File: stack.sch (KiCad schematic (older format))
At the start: 6 parts, among them U26 74LS245, U27 74LS173, U28 74LS173, U29 74LS245, U30 74LS173, U31 74LS173

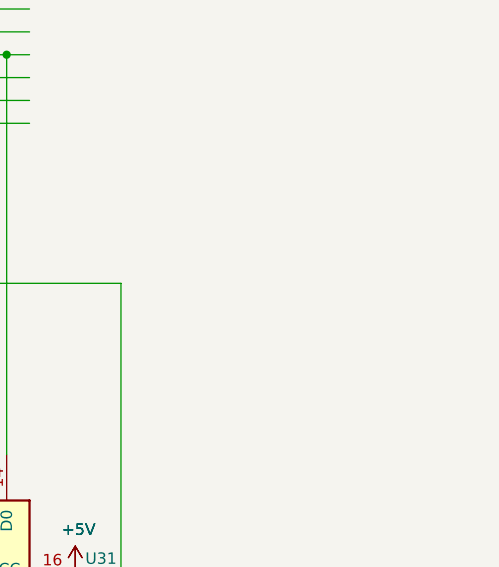
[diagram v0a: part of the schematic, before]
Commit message: added power caps
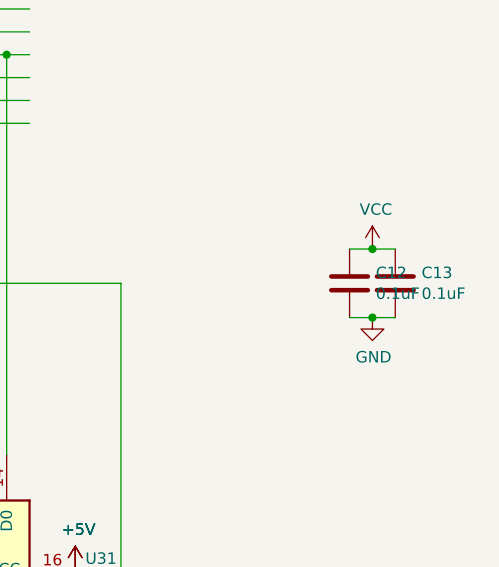
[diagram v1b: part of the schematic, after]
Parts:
- added C12, C13: 0.1uF, Capacitor_THT:CP_Axial_L10.0mm_D4.5mm_P15.00mm_Horizontal, symbol Device:C
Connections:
- net labels added: VCC
- wire segments 251 -> 255
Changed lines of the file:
@@
 $Descr A3 16535 11693
 encoding utf-8
-Sheet 9 21
+Sheet 8 21
 Title ""
 Date ""
@@
 Wire Wire Line
 	7600 3450 8900 3450
+$Comp
+L 16bitCpu-rescue:VCC-power #PWR?
+U 1 1 5FD411B2
+P 11350 2900
+AR Path="/5FD411B2" Ref="#PWR?"  Part="1"
+AR Path="/61968B9B/5FD411B2" Ref="#PWR0265"  Part="1"
+F 0 "#PWR0265" H 11350 2750 50  0001 C CNN
+F 1 "VCC" H 11365 3073 50  0000 C CNN
+F 2 "" H 11350 2900 50  0001 C CNN
+F 3 "" H 11350 2900 50  0001 C CNN
+	1    11350 2900
+	1    0    0    -1
+$EndComp
+$Comp
+L 16bitCpu-rescue:GND-power #PWR?
+U 1 1 5FD411B8
+P 11350 3200
+AR Path="/5FD411B8" Ref="#PWR?"  Part="1"
+AR Path="/5F75E433/5FD411B8" Ref="#PWR?"  Part="1"
+AR Path="/61968B9B/5FD411B8" Ref="#PWR0266"  Part="1"
+F 0 "#PWR0266" H 11350 2950 50  0001 C CNN
+F 1 "GND" H 11355 3027 50  0000 C CNN
+F 2 "" H 11350 3200 50  0001 C CNN
+F 3 "" H 11350 3200 50  0001 C CNN
+	1    11350 3200
+	1    0    0    -1
+$EndComp
+Wire Wire Line
+	11350 2900 11450 2900
+Wire Wire Line
+	11450 3200 11350 3200
+$Comp
+L Device:C C?
+U 1 1 5FD411C0
+P 11250 3050
+AR Path="/5F75E433/5FD411C0" Ref="C?"  Part="1"
+AR Path="/61968B9B/5FD411C0" Ref="C12"  Part="1"
+F 0 "C12" H 11365 3096 50  0000 L CNN
+F 1 "0.1uF" H 11365 3005 50  0000 L CNN
+F 2 "Capacitor_THT:CP_Axial_L10.0mm_D4.5mm_P15.00mm_Horizontal" H 11288 2900 50  0001 C CNN
+F 3 "" H 11250 3050 50  0001 C CNN
+	1    11250 3050
+	1    0    0    -1
+$EndComp
+Wire Wire Line
+	11350 2900 11250 2900
+Connection ~ 11350 2900
+Wire Wire Line
+	11250 3200 11350 3200
+Connection ~ 11350 3200
+$Comp
+L Device:C C?
+U 1 1 5FD411CA
+P 11450 3050
+AR Path="/5F75E433/5FD411CA" Ref="C?"  Part="1"
+AR Path="/61968B9B/5FD411CA" Ref="C13"  Part="1"
+F 0 "C13" H 11565 3096 50  0000 L CNN
+F 1 "0.1uF" H 11565 3005 50  0000 L CNN
+F 2 "Capacitor_THT:CP_Axial_L10.0mm_D4.5mm_P15.00mm_Horizontal" H 11488 2900 50  0001 C CNN
+F 3 "" H 11450 3050 50  0001 C CNN
+	1    11450 3050
+	1    0    0    -1
+$EndComp
 $EndSCHEMATC

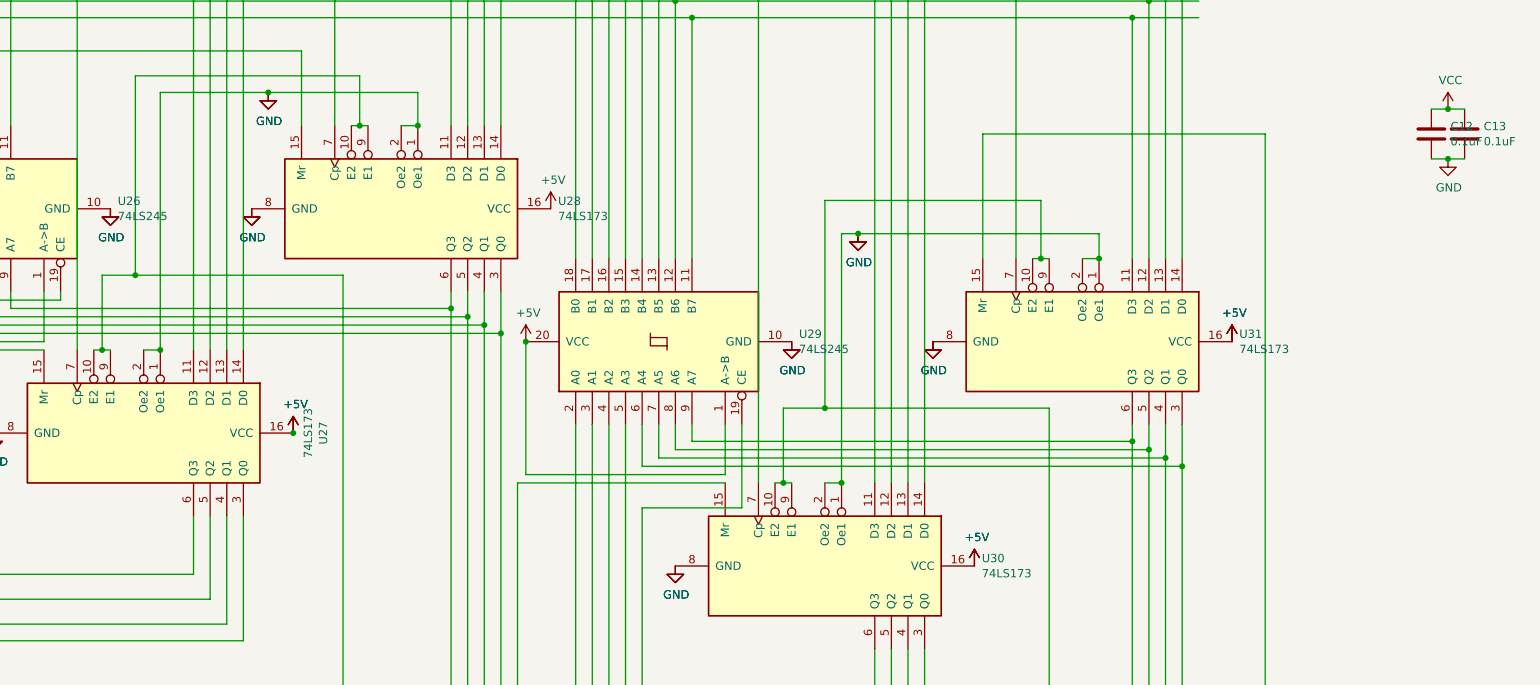
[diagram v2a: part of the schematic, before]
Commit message: added display
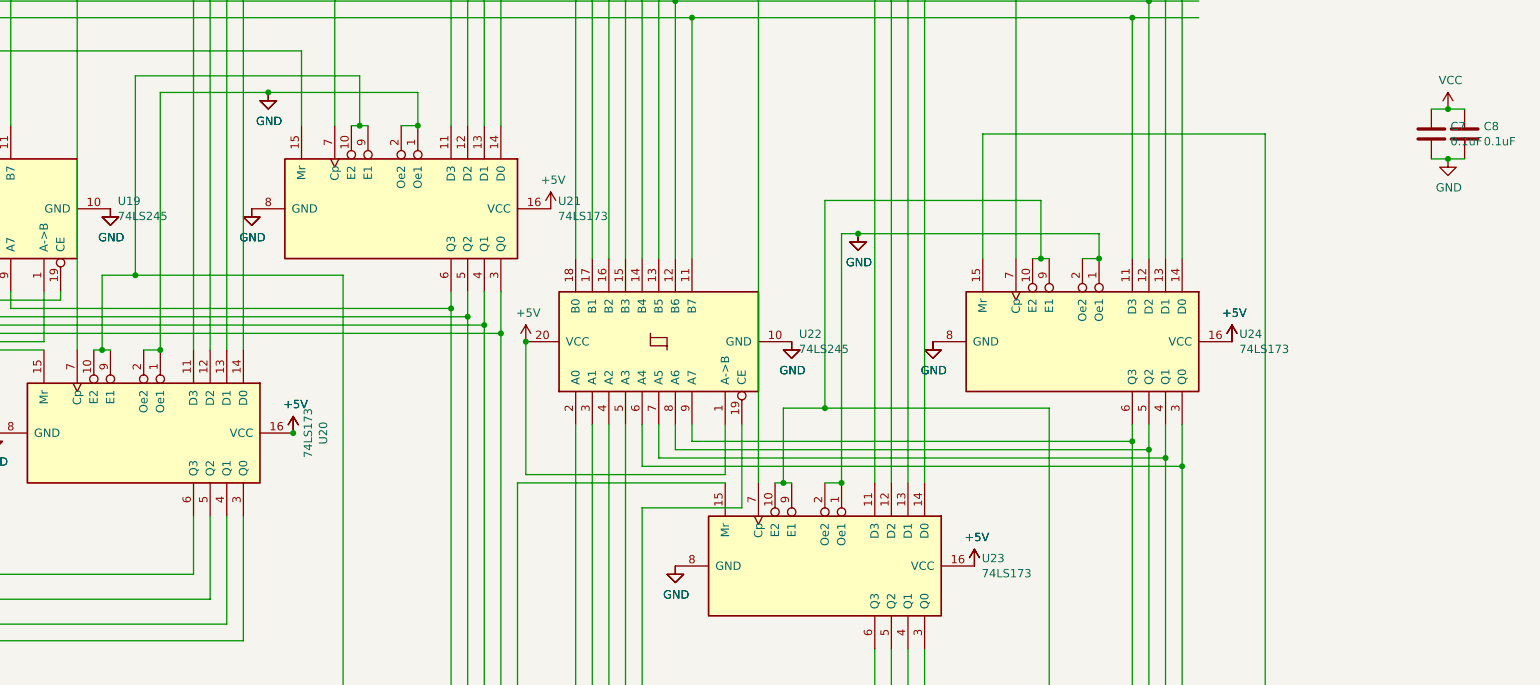
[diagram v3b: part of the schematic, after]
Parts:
- renumbered C12 to C7, C13 to C8, U26 to U19, U27 to U20, U28 to U21, U29 to U22, U30 to U23, U31 to U24

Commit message: clean up
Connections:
- wire segments 255 -> 236
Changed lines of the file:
@@
 Wire Wire Line
 	3800 4350 3800 1150
-Connection ~ 3800 1150
-Connection ~ 3900 1050
-Connection ~ 4000 950
-Connection ~ 4100 850
-Wire Wire Line
-	3900 1050 9850 1050
-Wire Wire Line
-	3800 1150 9850 1150
-Wire Wire Line
-	4000 950  9850 950
-Wire Wire Line
-	4100 850  9850 850
-Connection ~ 5350 1550
-Connection ~ 5450 1450
-Connection ~ 5550 1350
-Connection ~ 5650 1250
-Wire Wire Line
-	5650 1250 9850 1250
-Wire Wire Line
-	5550 1350 9850 1350
-Wire Wire Line
-	5450 1450 9850 1450
-Wire Wire Line
-	5350 1550 9850 1550
 Wire Wire Line
 	1300 1750 6200 1750
@@
 Wire Wire Line
 	6800 2350 9450 2350
-Connection ~ 7900 1950
-Wire Wire Line
-	7900 1950 9850 1950
-Connection ~ 8000 1850
-Wire Wire Line
-	8000 1850 9850 1850
-Connection ~ 8100 1750
-Wire Wire Line
-	8100 1750 9850 1750
-Connection ~ 8200 1650
-Wire Wire Line
-	8200 1650 9850 1650
-Connection ~ 9450 2350
-Wire Wire Line
-	9450 2350 9850 2350
-Connection ~ 9550 2250
-Wire Wire Line
-	9550 2250 9850 2250
-Connection ~ 9650 2150
-Wire Wire Line
-	9650 2150 9850 2150
-Connection ~ 9750 2050
-Wire Wire Line
-	9750 2050 9850 2050
 Wire Wire Line
 	8100 6150 8100 6800
@@
 Wire Wire Line
 	8750 3800 8750 600
-Connection ~ 8750 600
-Wire Wire Line
-	8750 600  9850 600
 Wire Wire Line
 	4650 3000 4650 600
@@
 Wire Wire Line
 	7100 4800 7100 5300
-Connection ~ 6500 8600
-Wire Wire Line
-	6500 8600 10200 8600
 $Comp
 L 16bitCpu-rescue:74LS173-74xx U?
@@
 Wire Wire Line
 	4700 8100 8950 8100
-Connection ~ 8950 8100
-Wire Wire Line
-	8950 8100 10200 8100
 Wire Wire Line
 	7700 3650 7700 5150
